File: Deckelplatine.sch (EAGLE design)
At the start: 61 parts, among them IC1 MAX1487EESA+, IC2 74HCT595D, IC3 74HCT595D, IC4 74HCT595D, IC5 74HCT595D, IC6 74HCT595D, J1 52808-2570, Q1 BC846BSMD, Q2 BC846BSMD, U1 LM2676S, X1 236-404, X2 233-502

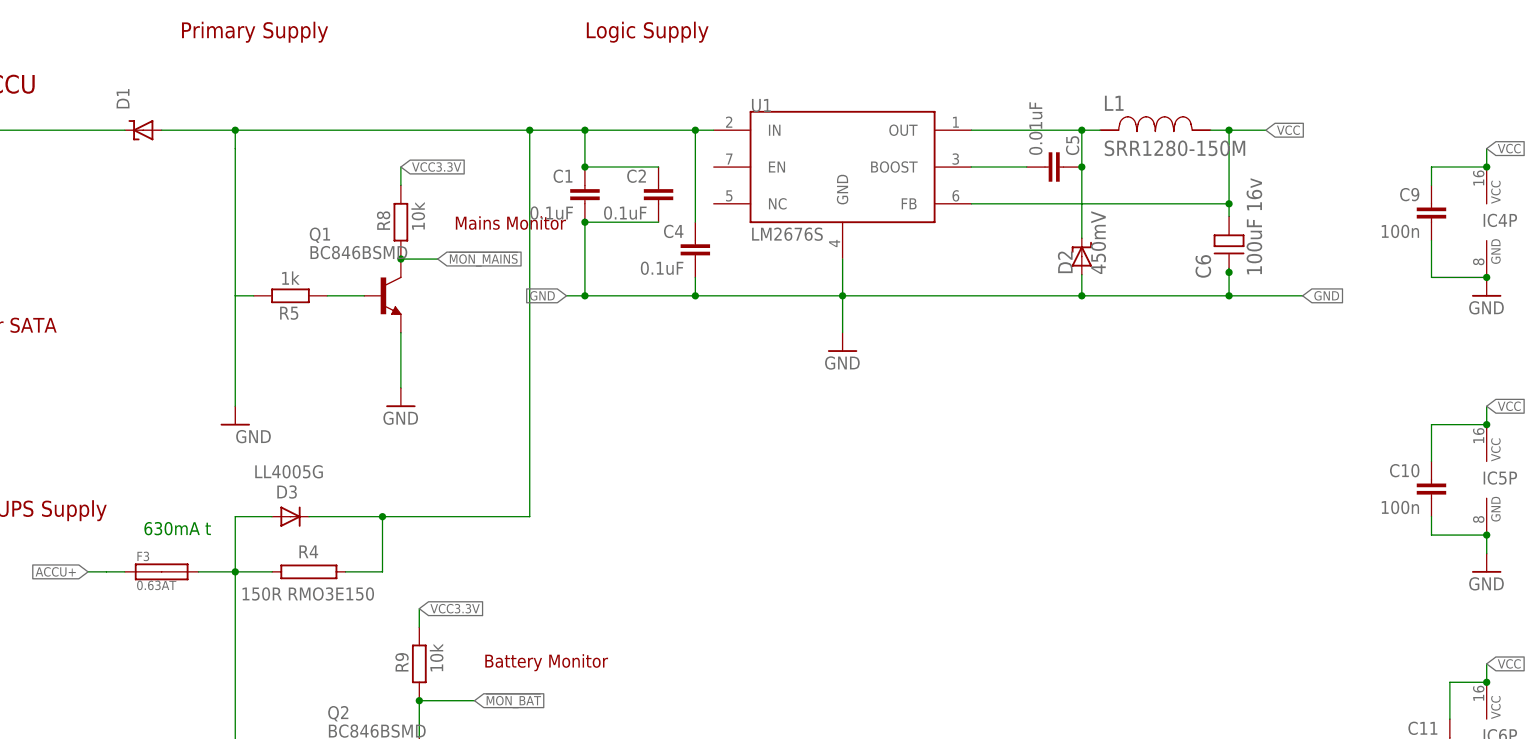
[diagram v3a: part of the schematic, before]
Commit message: Widerstand 150Ohm, 4Watt ausgetauscht
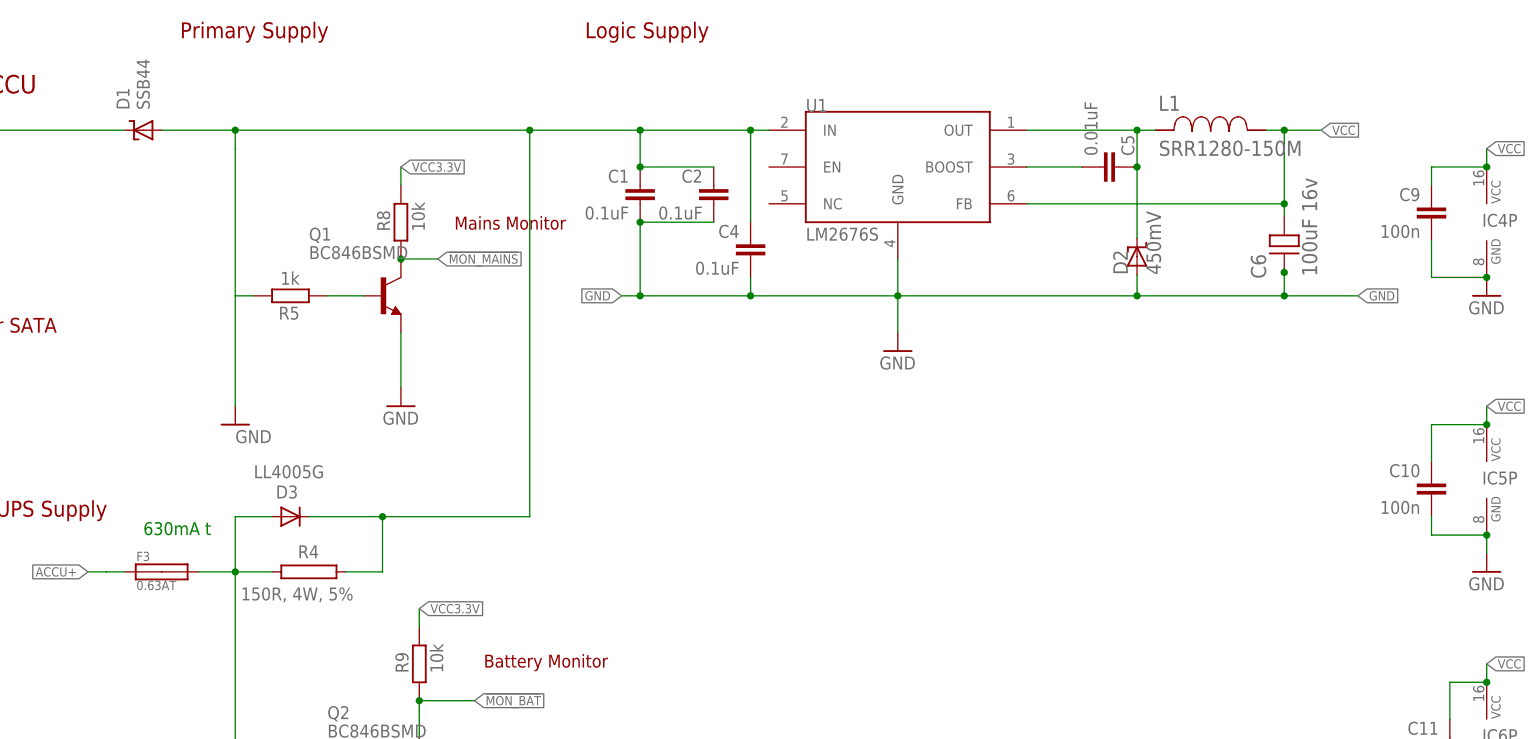
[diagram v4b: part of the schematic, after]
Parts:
- D1: value (none) -> SSB44
- R4: value 150R RMO3E150 -> 150R, 4W, 5%; OC_FARNELL_ALTERNATIVE 1735096 -> 1219280
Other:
- moved on the sheet: C1, C2, C4, C5, C6, D2, L1, U1

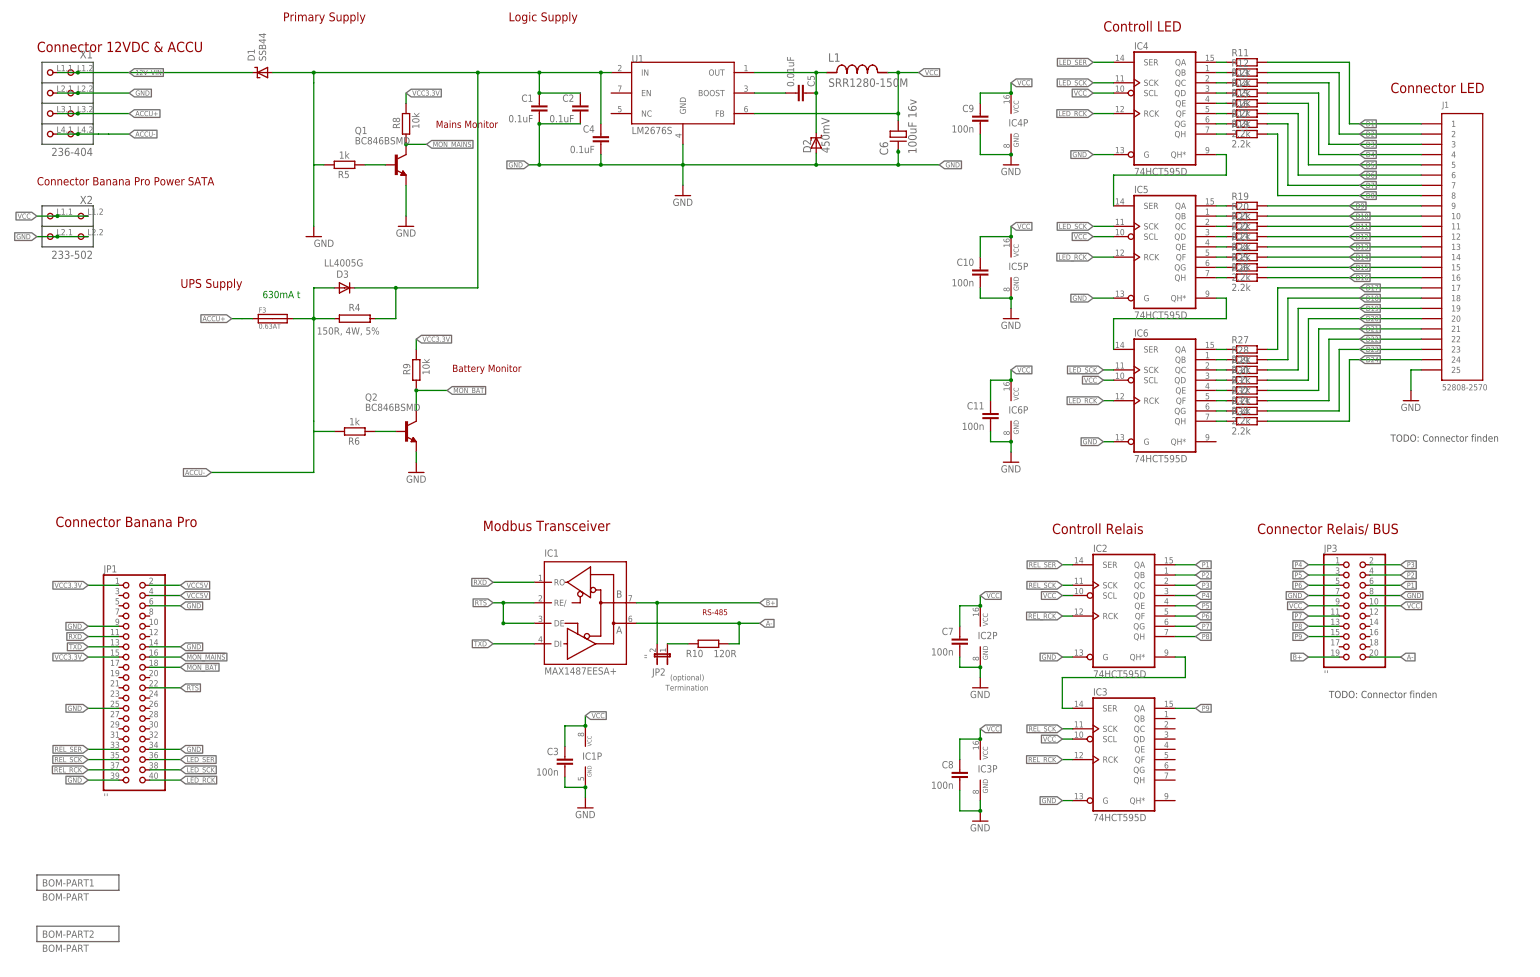
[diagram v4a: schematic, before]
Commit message: Schema, Board Layout und Routing komplett
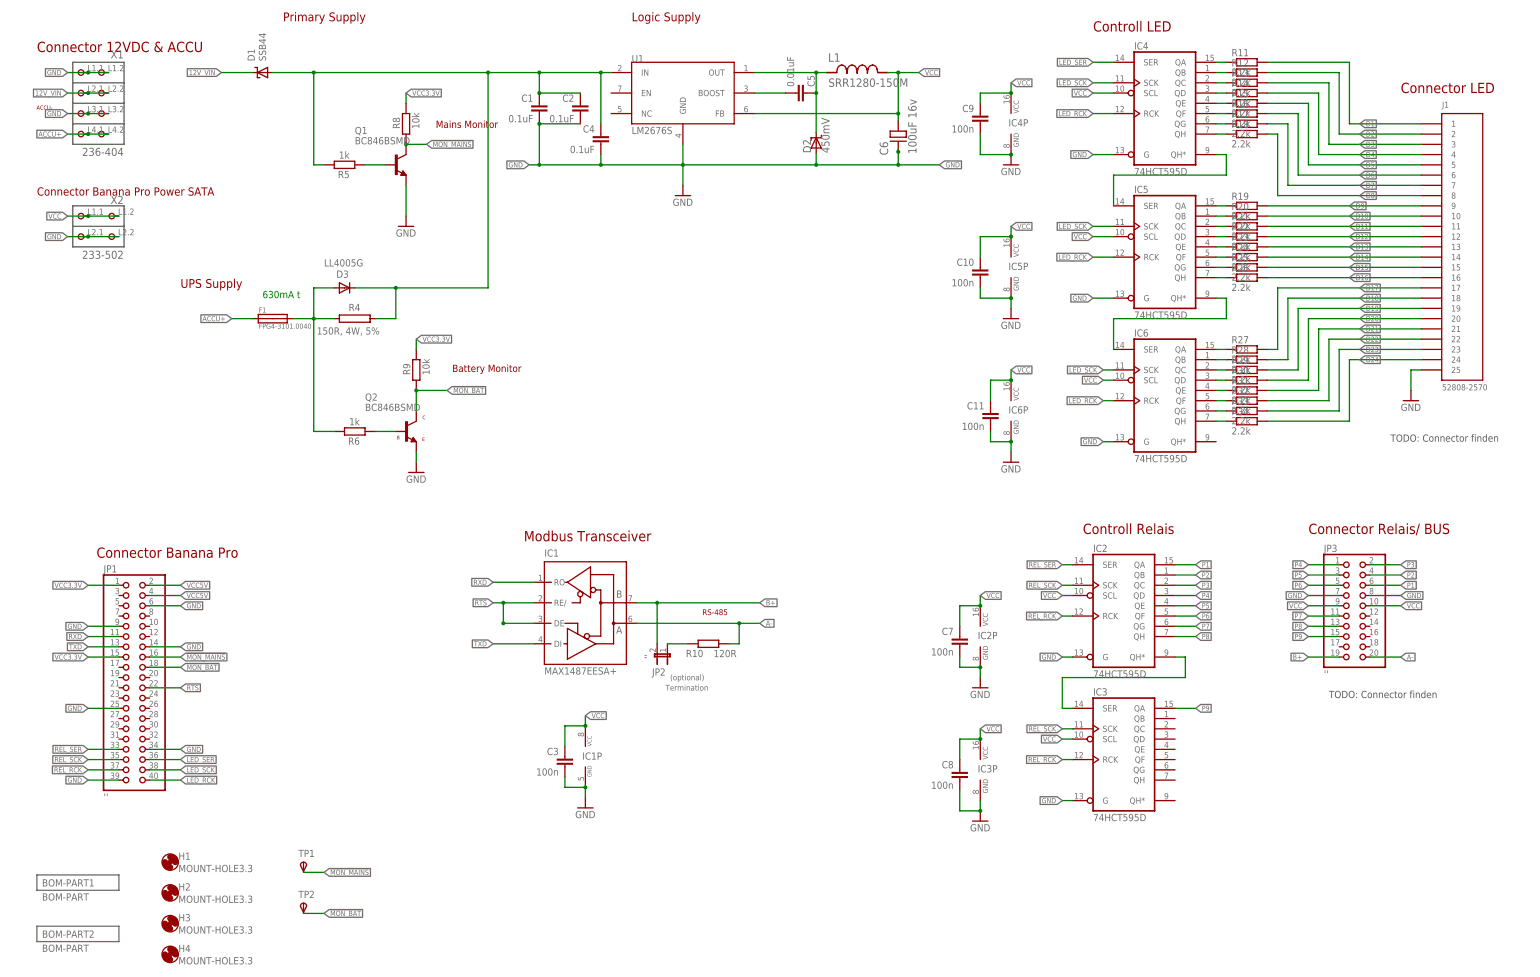
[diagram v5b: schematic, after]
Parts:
- added H1, H2, H3, H4: MOUNT-HOLE3.3, holes:MOUNT-HOLE3.3
- added TP1, TP2: TPSB1,27, testpad:TPSB1,27
- F1: value 0.63AT -> FPG4-3101.0040; MF SCHURTER -> (none); MPN 3101.0040 -> (none); OC_FARNELL 1222690 -> (none)
- renumbered F3 to F1
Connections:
- removed net ACCU-: X1.P4.1, X1.P4.2
- removed net N$38: D3.A, F1.P$2, R4.1
- removed net N$39: F1.P$1
- removed net V+: D3.C, R4.2
- net !MON_BAT: now also TP2.PP; no longer R6.2
- net !MON_MAINS: now also TP1.PP; no longer R5.2
- net 12V_VIN: now also D3.C, R4.2, R5.2, X1.P2.1, X1.P2.2; no longer X1.P1.1, X1.P1.2
- net ACCU+: now also D3.A, F1.P$1, F1.P$2, R4.1, R6.2, X1.P4.1, X1.P4.2; no longer X1.P3.1, X1.P3.2
- net GND: now also X1.P1.1, X1.P1.2, X1.P3.1, X1.P3.2; no longer X1.P2.1, X1.P2.2
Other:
- note added: "ACCU-"
- note added: "B"
- note added: "C"
- note added: "E"
- moved on the sheet: X1, X2

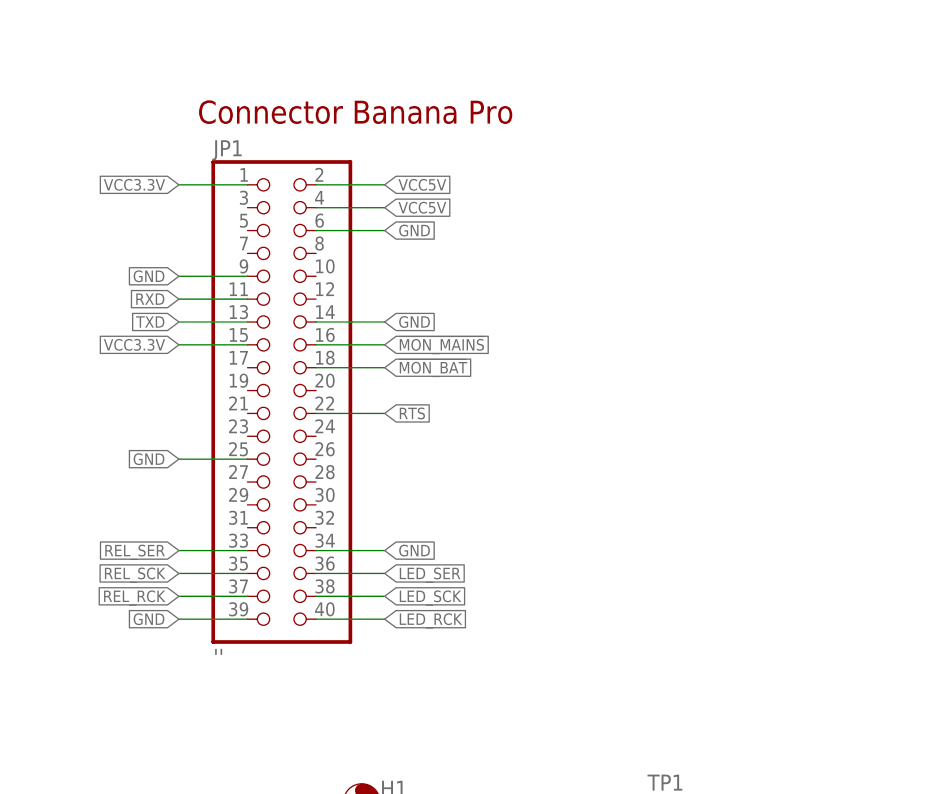
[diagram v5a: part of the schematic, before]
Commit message: Autorouter mit 7 Airwire left
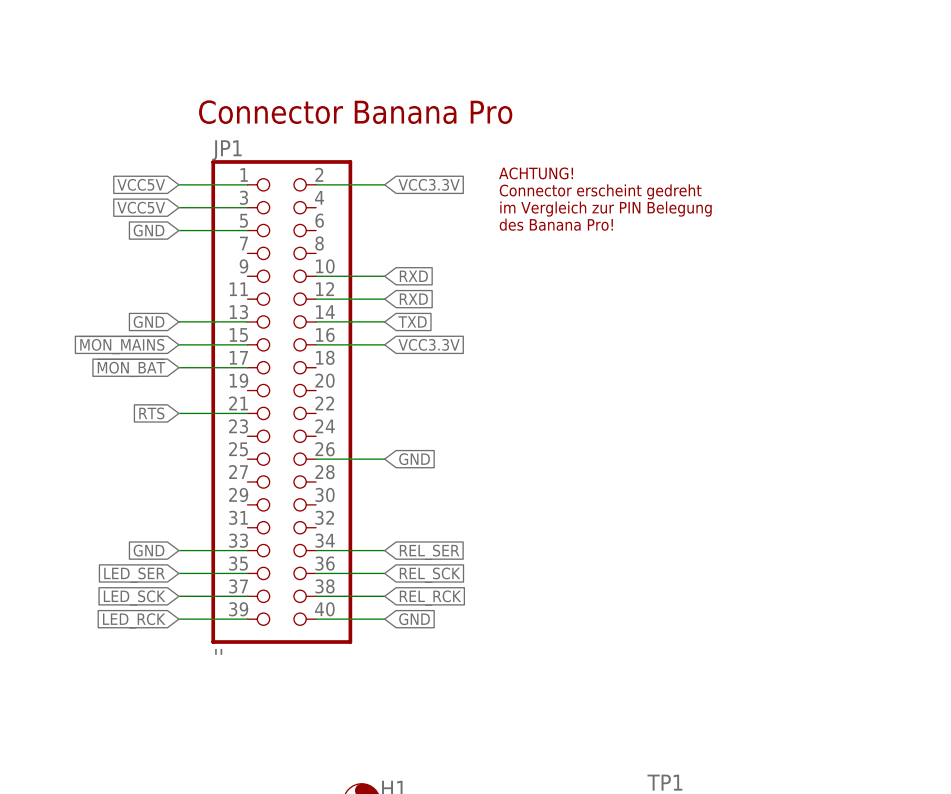
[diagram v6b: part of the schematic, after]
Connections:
- new net N$1415: JP1.12
- net !MON_BAT: now also JP1.17; no longer JP1.18
- net !MON_MAINS: now also JP1.15; no longer JP1.16
- net GND: now also JP1.13, JP1.26, JP1.33, JP1.40, JP1.5; no longer JP1.14, JP1.25, JP1.34, JP1.39, JP1.6, JP1.9
- net LED_RCK: now also JP1.39; no longer JP1.40
- net LED_SCK: now also JP1.37; no longer JP1.38
- net LED_SER: now also JP1.35; no longer JP1.36
- net REL_RCK: now also JP1.38; no longer JP1.37
- net REL_SCK: now also JP1.36; no longer JP1.35
- net REL_SER: now also JP1.34; no longer JP1.33
- net RTS: now also JP1.21; no longer JP1.22
- net RXD: now also JP1.10; no longer JP1.11
- net TXD: now also JP1.14; no longer JP1.13
- net VCC3.3V: now also JP1.16, JP1.2; no longer JP1.1, JP1.15
- net VCC5V: now also JP1.1, JP1.3; no longer JP1.2, JP1.4
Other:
- note added: "ACHTUNG! Connector erscheint gedreht im Vergleich zur PIN Belegung des Banana Pro!"

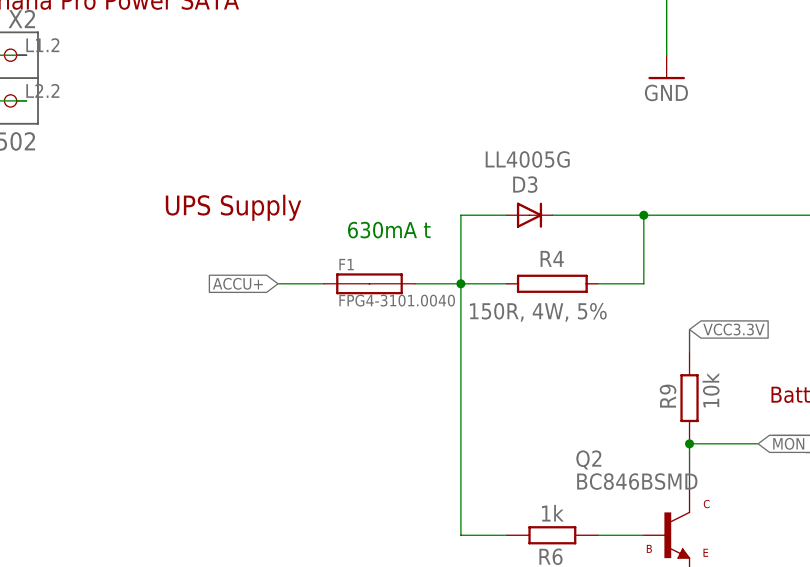
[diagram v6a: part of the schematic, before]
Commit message: Erste ferige Version nach Tausch der Sicherung
Board Layout, Schema, dicke Power Lines, neue Sicherung
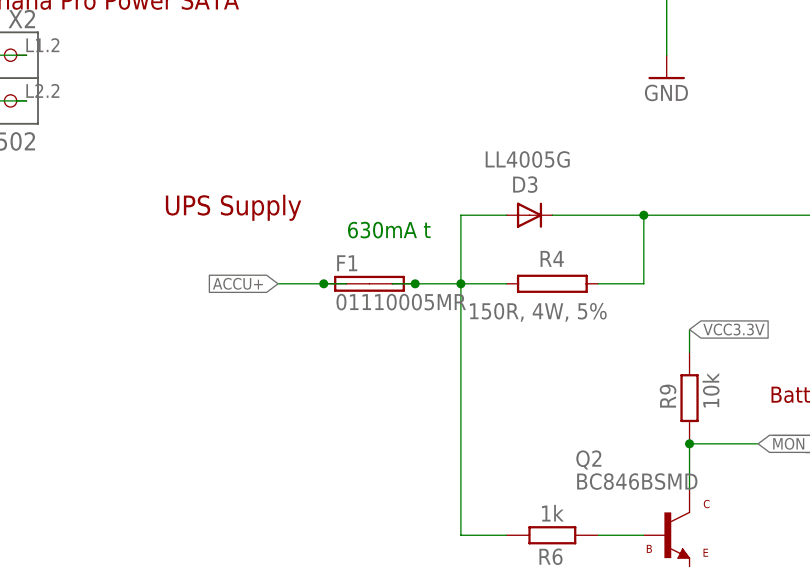
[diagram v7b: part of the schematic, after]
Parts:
- F1: value FPG4-3101.0040 -> 01110005MR; device fuse-schurter:FPG4-3101.0040 -> fuse-littlefuse:01110005MR
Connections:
- net ACCU+: now also F1.1A, F1.1B, F1.2A, F1.2B; no longer F1.P$1, F1.P$2
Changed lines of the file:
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@@
 <attribute name="PROJEKTNAME" value="xMZ_Mod Touch"/>
 <attribute name="REV" value="A"/>
-<attribute name="VERSION" value="0.1"/>
+<attribute name="VERSION" value="0.1.0"/>
 </attributes>
 <variantdefs>
@@
 <part name="H3" library="holes" deviceset="MOUNT-HOLE" device="3.3"/>
 <part name="H4" library="holes" deviceset="MOUNT-HOLE" device="3.3"/>
-<part name="F1" library="fuse-schurter" deviceset="FPG4-3101.0040" device=""/>
+<part name="F1" library="fuse-littlefuse" deviceset="01110005MR" device=""/>
 <part name="TP1" library="testpad" deviceset="TPS" device="B1,27" value="TPSB1,27"/>
 <part name="TP2" library="testpad" deviceset="TPS" device="B1,27" value="TPSB1,27"/>
@@
 <net name="ACCU+" class="0">
 <segment>
-<pinref part="F1" gate="G$1" pin="P$1"/>
+<pinref part="F1" gate="G$1" pin="1A"/>
 <wire x1="66.04" y1="172.72" x2="60.96" y2="172.72" width="0.1524" layer="91"/>
 <label x="60.96" y="172.72" size="1.27" layer="95" rot="R180" xref="yes"/>
+<pinref part="F1" gate="G$1" pin="1B"/>
+<wire x1="66.04" y1="172.72" x2="68.58" y2="172.72" width="0.1524" layer="91"/>
+<junction x="66.04" y="172.72"/>
 </segment>
 <segment>
@@
 <wire x1="86.36" y1="172.72" x2="81.28" y2="172.72" width="0.1524" layer="91"/>
 <wire x1="81.28" y1="172.72" x2="81.28" y2="180.34" width="0.1524" layer="91"/>
-<pinref part="F1" gate="G$1" pin="P$2"/>
+<pinref part="F1" gate="G$1" pin="2A"/>
 <wire x1="76.2" y1="172.72" x2="81.28" y2="172.72" width="0.1524" layer="91"/>
 <junction x="81.28" y="172.72"/>
@@
 <pinref part="R6" gate="G$1" pin="2"/>
 <wire x1="81.28" y1="144.78" x2="86.36" y2="144.78" width="0.1524" layer="91"/>
-</segment>
-</net>
+<pinref part="F1" gate="G$1" pin="2B"/>
+<wire x1="76.2" y1="172.72" x2="73.66" y2="172.72" width="0.1524" layer="91"/>
+<junction x="76.2" y="172.72"/>
+</segment>
+</net>
